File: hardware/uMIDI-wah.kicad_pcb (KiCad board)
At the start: 2 copper layers, 45 x 24 mm, 44 parts, among them Q1 BSS138, U1 TL071CPSR, X1 9V, X2 uMIDI, X3 Input, X4 Output

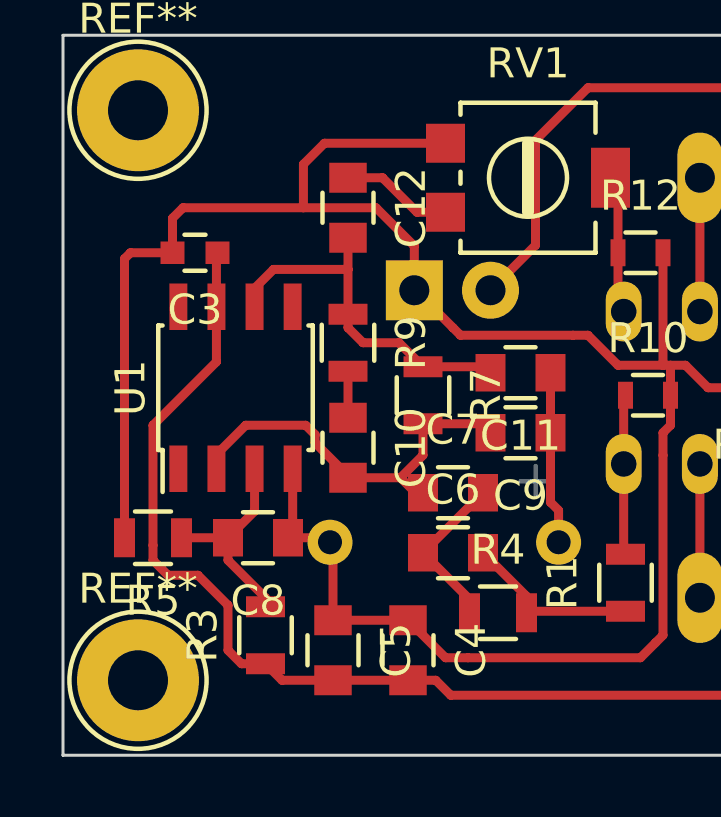
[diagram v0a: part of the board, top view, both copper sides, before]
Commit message: Fix SOIC package width
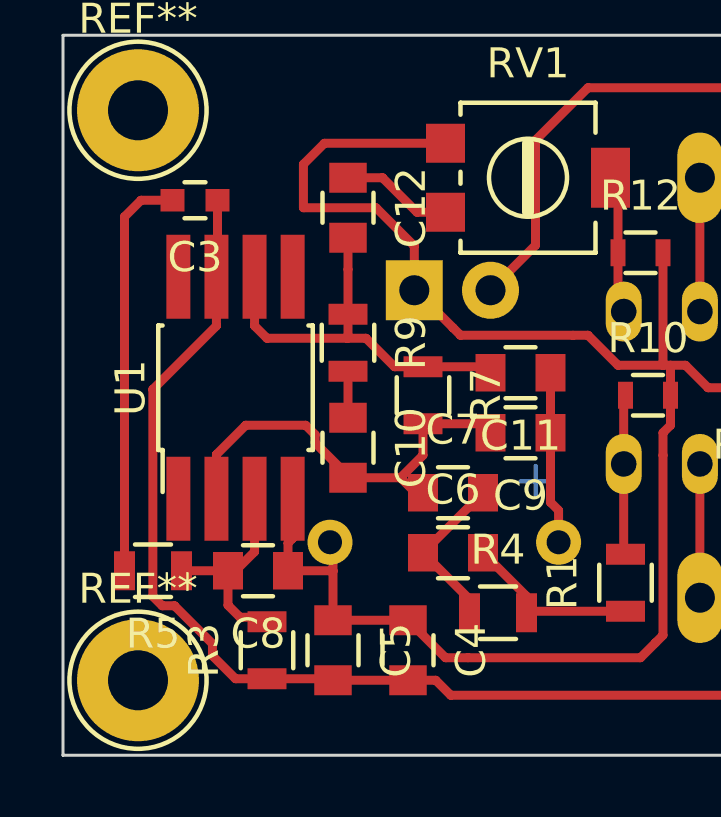
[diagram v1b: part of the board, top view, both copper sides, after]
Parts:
- moved C3 1.75 mm to (184.4, 131.5)
- moved C8 1.10 mm to (186.5, 143.8)
- moved R5 1.10 mm to (183.0, 143.8)
- moved R3 0.50 mm to (186.8, 146.5)
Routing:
- net +9V: track 48.2 -> 51.7 mm
- net Net-(C8-Pad2): track 7.16 -> 9.56 mm
- net GND: track 158.0 -> 155.9 mm
- net Net-(C11-Pad2): track 12.3 -> 13.0 mm

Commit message: Increase pcb size; Add label
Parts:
- added R16: 4.7k, Resistors_SMD:R_0805, F.Cu at (197.0, 123.0)
- C11: value 2n -> 2.2n
- C7: value 47n -> 4.7n
- RV1: value 10k -> 5k
- moved C1 2.00 mm to (208.8, 145.8)
- moved C10 2.00 mm to (191.5, 139.8)
- moved C11 2.00 mm to (197.2, 137.2)
- moved C12 2.00 mm to (191.5, 131.8)
- moved C13 2.00 mm to (214.5, 142.8)
- moved C14 2.00 mm to (210.2, 141.8)
- moved C15 2.00 mm to (218.0, 129.5)
- moved C2 2.00 mm to (210.8, 145.8)
- moved C3 2.00 mm to (186.4, 131.5)
- moved C4 2.00 mm to (193.5, 146.5)
- moved C5 2.00 mm to (191.0, 146.5)
- moved C6 2.00 mm to (195.0, 143.2)
- moved C7 2.00 mm to (195.0, 141.2)
- moved C8 2.00 mm to (188.5, 143.8)
- moved C9 2.00 mm to (197.2, 139.2)
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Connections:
- RV1 pad 1: Net-(C12-Pad1) -> Net-(R16-Pad1)
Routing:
- net Net-(C12-Pad1): track 3.73 -> 0.00 mm
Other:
- board size 45 x 24 mm -> 50 x 24 mm
- board text added: "uMIDI-Wah v0.3"

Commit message: Place and route
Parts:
- removed D1: LED, LEDs:LED-5MM
- removed R2: 82, Resistors_SMD:R_0603
- removed the REF** at (182.5, 147.5)
- removed the REF** at (182.5, 128.5)
- added X5: Enable, Connect:PINHEAD1-2, B.Cu at (223.5, 133.0)
- X2: value uMIDI -> PWM; footprint uMIDI-wah:VASCH5x2_diy-pcb -> Connect:PINHEAD1-2
- moved X2 33.4 mm to (190.0, 129.2), turned to 0 degrees
- moved R6 26.8 mm to (194.2, 129.2), turned to 180 degrees
- moved C15 17.3 mm to (201.5, 134.8), turned to 90 degrees
- moved R15 15.1 mm to (199.5, 134.2), turned to 90 degrees
- moved C1 11.2 mm to (219.5, 142.5), turned to 90 degrees
- moved R16 9.52 mm to (194.8, 132.2)
- moved X1 9.34 mm to (223.5, 143.0), turned to 90 degrees
- moved R14 4.85 mm to (219.0, 132.8), turned to 270 degrees
- moved C2 4.78 mm to (215.5, 146.2), turned to 180 degrees
- moved R4 4.78 mm to (201.2, 144.8), turned to 270 degrees
- moved C6 4.04 mm to (198.8, 144.8), turned to 270 degrees
- moved X4 3.81 mm to (208.0, 129.2)
- moved X3 3.50 mm to (208.0, 144.8)
- moved RV1 3.09 mm to (200.5, 130.0)
- moved R1 3.04 mm to (203.8, 144.8)
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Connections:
- X2 pad 1: (no net) -> GND
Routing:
- net GND: track 155.9 -> 198.5 mm
- net Net-(D2-Pad2): track 21.7 -> 2.35 mm
- net +9V: track 51.7 -> 66.9 mm
- net Net-(C15-Pad2): track 8.10 -> 13.8 mm
- net Net-(C11-Pad2): track 13.0 -> 16.9 mm
- net Net-(C10-Pad2): track 13.2 -> 17.0 mm
- net Net-(C8-Pad2): track 9.56 -> 13.1 mm
- net Net-(C12-Pad1): track 0.00 -> 3.11 mm
- net Net-(D1-Pad2): track 2.85 -> 0.00 mm
- net Net-(R16-Pad1): track 0.00 -> 2.68 mm
- net /True bypass/Loop_Out: track 4.46 -> 6.42 mm
- net /True bypass/relais_p: track 5.78 -> 7.16 mm
- net Net-(C10-Pad1): track 1.55 -> 2.77 mm
- net Net-(C6-Pad2): track 5.92 -> 5.02 mm
- net Net-(C11-Pad1): track 5.76 -> 5.09 mm
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
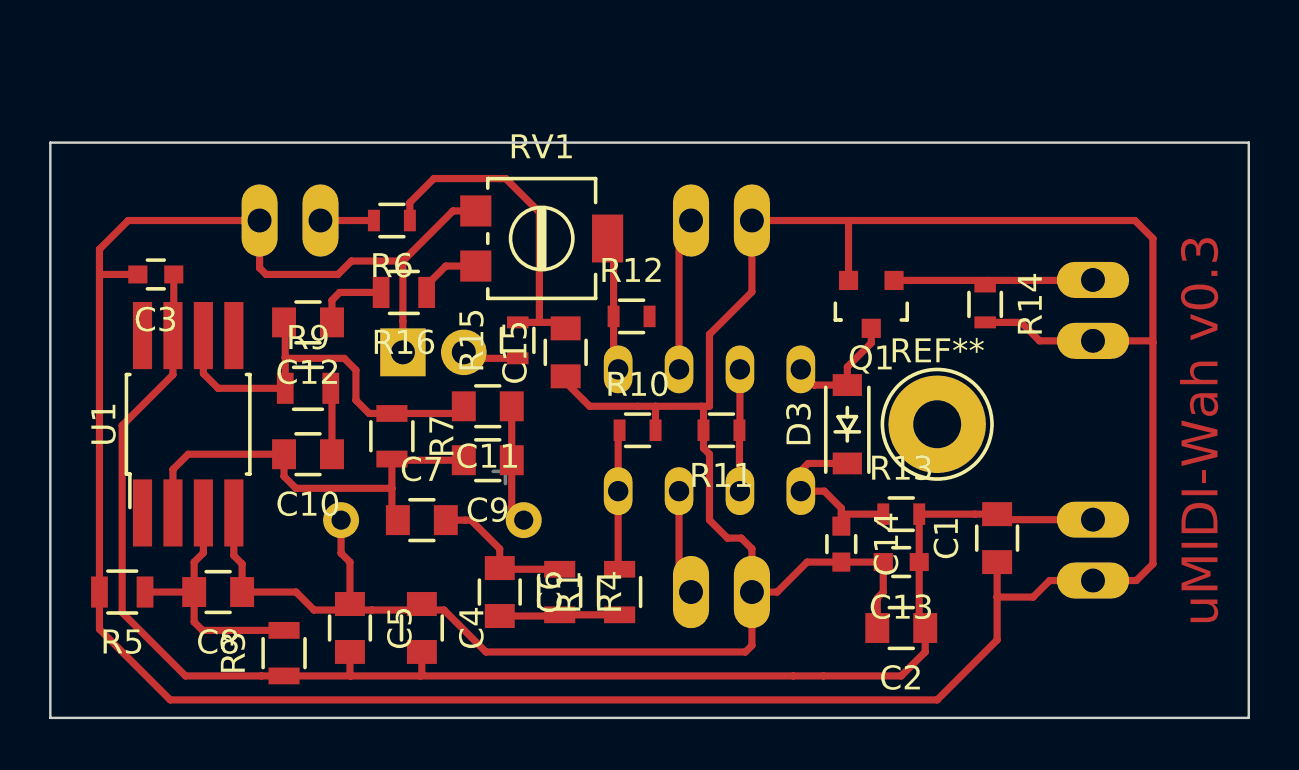
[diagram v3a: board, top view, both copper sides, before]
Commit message: Increase trace widths
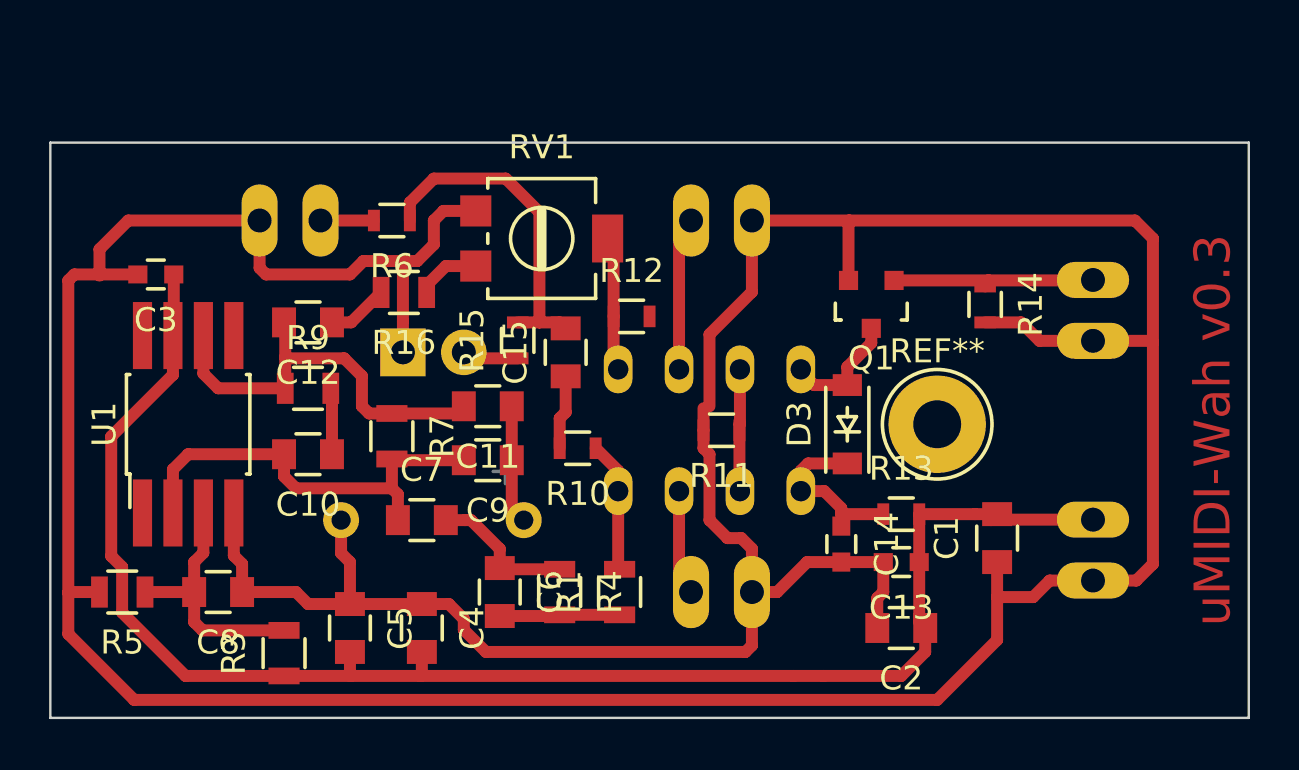
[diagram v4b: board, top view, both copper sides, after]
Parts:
- moved R10 2.61 mm to (202.0, 138.8), turned to 180 degrees
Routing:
- net Net-(C12-Pad1): track 3.11 -> 2.57 mm
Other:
- net class Default: trace_width 0.3 -> 0.5

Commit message: Add 9V polarity protection diode
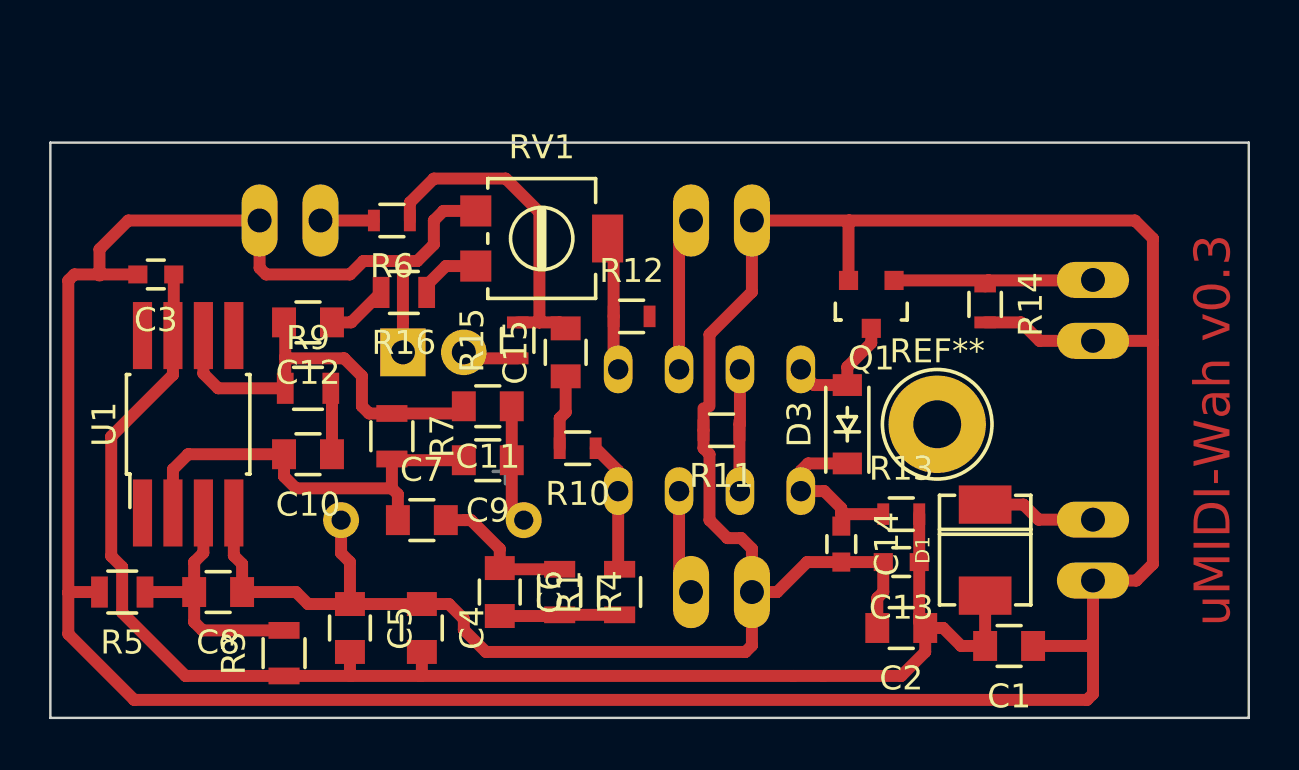
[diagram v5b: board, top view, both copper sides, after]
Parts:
- added D1: B160-13-F, uMIDI:DO-214-AC_SMA, F.Cu at (219.0, 143.0)
- moved C1 4.53 mm to (220.0, 147.0), turned to 180 degrees
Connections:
- X1 pad 2: +9V -> Net-(D1-Pad2)
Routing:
- net Net-(D1-Pad2): track 0.00 -> 4.76 mm
- net GND: track 198.1 -> 200.9 mm
- net +9V: track 67.3 -> 64.5 mm
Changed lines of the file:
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@@
 (kicad_pcb (version 4) (host pcbnew "(2015-09-12 BZR 6188)-product")
   (general
-    (links 72)
+    (links 73)
     (no_connects 0)
     (area 179.949999 125.949999 230.050001 150.050001)
     (thickness 1.6)
     (drawings 7)
-    (tracks 218)
+    (tracks 219)
     (zones 0)
-    (modules 42)
-    (nets 23)
+    (modules 43)
+    (nets 24)
   )
   (page A4)
@@
   (net 21 "Net-(C15-Pad2)")
   (net 22 "Net-(R16-Pad1)")
+  (net 23 "Net-(D1-Pad2)")
   (net_class Default "This is the default net class."
     (clearance 0.3)
@@
     (add_net "Net-(C6-Pad2)")
     (add_net "Net-(C8-Pad2)")
+    (add_net "Net-(D1-Pad2)")
     (add_net "Net-(D2-Pad2)")
     (add_net "Net-(R16-Pad1)")
@@
       (net 1 GND))
     (pad 2 thru_hole oval (at 1.27 0 90) (size 1.50622 3.01498) (drill 0.99822) (layers *.Cu *.Mask)
-      (net 2 +9V))
+      (net 23 "Net-(D1-Pad2)"))
   )
   (module Connect:PINHEAD1-2 (layer B.Cu)
@@
   )
   (module Capacitors_SMD:C_0805 (layer F.Cu)
-    (at 219.5 142.5 90)
+    (at 220 147 180)
     (descr "Capacitor SMD 0805, reflow soldering, AVX (see smccp.pdf)")
     (tags "capacitor 0805")
     (attr smd)
-    (fp_text reference C1 (at 0 -2.1 90) (layer F.SilkS)
-      (effects (font (size 1 1) (thickness 0.15)))
-    )
-    (fp_text value 10u (at 0 2.1 90) (layer F.Fab)
+    (fp_text reference C1 (at 0 -2.1 180) (layer F.SilkS)
+      (effects (font (size 1 1) (thickness 0.15)))
+    )
+    (fp_text value 10u (at 0 2.1 180) (layer F.Fab)
       (effects (font (size 1 1) (thickness 0.15)))
     )
@@
     (fp_line (start 0.5 -0.85) (end -0.5 -0.85) (layer F.SilkS) (width 0.15))
     (fp_line (start -0.5 0.85) (end 0.5 0.85) (layer F.SilkS) (width 0.15))
-    (pad 1 smd rect (at -1 0 90) (size 1 1.25) (layers F.Cu F.Paste F.Mask)
-      (net 1 GND))
-    (pad 2 smd rect (at 1 0 90) (size 1 1.25) (layers F.Cu F.Paste F.Mask)
+    (pad 1 smd rect (at -1 0 180) (size 1 1.25) (layers F.Cu F.Paste F.Mask)
+      (net 1 GND))
+    (pad 2 smd rect (at 1 0 180) (size 1 1.25) (layers F.Cu F.Paste F.Mask)
       (net 2 +9V))
     (model Capacitors_SMD.3dshapes/C_0805.wrl
@@
       (net 16 /PWM))
   )
+  (module uMIDI:DO-214-AC_SMA placed (layer F.Cu)
+    (at 219 143 90)
+    (descr "DO-214AC (SMA)  PACKAGE.")
+    (tags DO-214AC_SMA)
+    (attr smd)
+    (fp_text reference D1 (at 0 -2.60096 90) (layer F.SilkS)
+      (effects (font (size 0.6 0.6) (thickness 0.1143)))
+    )
+    (fp_text value B160-13-F (at 0 2.79908 90) (layer F.SilkS) hide
+      (effects (font (size 1.00076 1.00076) (thickness 0.11938)))
+    )
+    (fp_line (start -2.286 -1.905) (end 2.286 -1.905) (layer F.SilkS) (width 0.15))
+    (fp_line (start 2.286 -1.905) (end 2.286 -1.27) (layer F.SilkS) (width 0.15))
+    (fp_line (start 0.6604 1.905) (end 0.6604 -1.905) (layer F.SilkS) (width 0.15))
+    (fp_line (start 0.8636 1.905) (end 0.8636 -1.905) (layer F.SilkS) (width 0.15))
+    (fp_line (start -2.286 1.27) (end -2.286 1.905) (layer F.SilkS) (width 0.15))
+    (fp_line (start -2.286 1.905) (end 2.286 1.905) (layer F.SilkS) (width 0.15))
+    (fp_line (start 2.286 1.905) (end 2.286 1.27) (layer F.SilkS) (width 0.15))
+    (fp_line (start -2.286 -1.27) (end -2.286 -1.905) (layer F.SilkS) (width 0.15))
+    (pad 1 smd rect (at -1.89992 0 90) (size 1.6002 2.19964) (layers F.Cu F.Paste F.Mask)
+      (net 2 +9V))
+    (pad 2 smd rect (at 1.89992 0 90) (size 1.6002 2.19964) (layers F.Cu F.Paste F.Mask)
+      (net 23 "Net-(D1-Pad2)"))
+    (model smd/do214.wrl
+      (at (xyz 0 0 0))
+      (scale (xyz 0.95 0.95 0.95))
+      (rotate (xyz 0 0 0))
+    )
+  )
   (gr_text "uMIDI-Wah v0.3" (at 228.5 138 90) (layer F.Cu)
     (effects (font (size 1.5 1.5) (thickness 0.35)))
@@
   (gr_line (start 230 126) (end 180 126) (layer Edge.Cuts) (width 0.1))
   (gr_line (start 230 150) (end 180 150) (layer Edge.Cuts) (width 0.1))
+  (segment (start 221 147) (end 223.308637 147) (width 0.5) (layer F.Cu) (net 1))
+  (segment (start 223.308637 147) (end 223.5 146.808637) (width 0.5) (layer F.Cu) (net 1))
+  (segment (start 223.5 149) (end 223.5 146.808637) (width 0.5) (layer F.Cu) (net 1))
+  (segment (start 223.5 146.808637) (end 223.5 144.27) (width 0.5) (layer F.Cu) (net 1))
+  (segment (start 180.75 144.775008) (end 180.75 146.5) (width 0.5) (layer F.Cu) (net 1))
+  (segment (start 180.75 146.5) (end 183.5 149.25) (width 0.5) (layer F.Cu) (net 1))
+  (segment (start 183.5 149.25) (end 223.25 149.25) (width 0.5) (layer F.Cu) (net 1))
+  (segment (start 223.25 149.25) (end 223.5 149) (width 0.5) (layer F.Cu) (net 1))
   (segment (start 201.25 137.5) (end 201.5 137.25) (width 0.5) (layer F.Cu) (net 1))
   (segment (start 201.5 137.25) (end 201.5 135.75) (width 0.5) (layer F.Cu) (net 1))
@@
   (segment (start 198.175 147.25) (end 209 147.25) (width 0.5) (layer F.Cu) (net 1))
   (segment (start 192.5 145.25) (end 195.5 145.25) (width 0.5) (layer F.Cu) (net 1))
-  (segment (start 180.75 144.775008) (end 180.75 146.5) (width 0.5) (layer F.Cu) (net 1))
-  (segment (start 180.75 146.5) (end 183.5 149.25) (width 0.5) (layer F.Cu) (net 1))
-  (segment (start 183.5 149.25) (end 217 149.25) (width 0.5) (layer F.Cu) (net 1))
-  (segment (start 217 149.25) (end 219.5 146.75) (width 0.5) (layer F.Cu) (net 1))
-  (segment (start 219.5 146.75) (end 219.5 144.960213) (width 0.5) (layer F.Cu) (net 1))
   (segment (start 180.75 131.75) (end 180.75 144.775008) (width 0.5) (layer F.Cu) (net 1))
   (segment (start 182.05 144.75) (end 180.775008 144.75) (width 0.5) (layer F.Cu) (net 1))
@@
   (segment (start 194.71 130.94) (end 194.71 133.45) (width 0.5) (layer F.Cu) (net 1))
   (segment (start 194.71 133.45) (end 194.71 134.75) (width 0.5) (layer F.Cu) (net 1))
-  (segment (start 219.5 143.5) (end 219.5 144.960213) (width 0.5) (layer F.Cu) (net 1))
-  (segment (start 223.5 144.27) (end 221.69251 144.27) (width 0.5) (layer F.Cu) (net 1))
-  (segment (start 221.69251 144.27) (end 221.002297 144.960213) (width 0.5) (layer F.Cu) (net 1))
-  (segment (start 221.002297 144.960213) (end 219.5 144.960213) (width 0.5) (layer F.Cu) (net 1))
   (segment (start 182.05 131.546616) (end 182.05 130.45) (width 0.5) (layer F.Cu) (net 1))
   (segment (start 183.65 131.5) (end 182.096616 131.5) (width 0.5) (layer F.Cu) (net 1))
@@
   (segment (start 188 143.575) (end 187.655 143.23) (width 0.5) (layer F.Cu) (net 1))
   (segment (start 187.655 143.23) (end 187.655 140.45) (width 0.5) (layer F.Cu) (net 1))
+  (segment (start 219 147) (end 218 147) (width 0.5) (layer F.Cu) (net 2))
+  (segment (start 218 147) (end 217.25 146.25) (width 0.5) (layer F.Cu) (net 2))
+  (segment (start 217.25 146.25) (end 216.5 146.25) (width 0.5) (layer F.Cu) (net 2))
+  (segment (start 219 144.64992) (end 219 146.75) (width 0.5) (layer F.Cu) (net 2))
   (segment (start 189.75 148.25) (end 185.639998 148.25) (width 0.5) (layer F.Cu) (net 2))
   (segment (start 185.639998 148.25) (end 182.994999 145.605001) (width 0.5) (layer F.Cu) (net 2))
@@
   (segment (start 216.25 146) (end 216.5 146.25) (width 0.5) (layer F.Cu) (net 2))
   (segment (start 216.25 143.5) (end 216.25 141.5) (width 0.5) (layer F.Cu) (net 2))
-  (segment (start 219.5 141.5) (end 218.575 141.5) (width 0.5) (layer F.Cu) (net 2))
-  (segment (start 218.575 141.5) (end 216.25 141.5) (width 0.5) (layer F.Cu) (net 2))
-  (segment (start 219.25 141.75) (end 219.5 141.5) (width 0.5) (layer F.Cu) (net 2))
-  (segment (start 223.5 141.73) (end 219.73 141.73) (width 0.5) (layer F.Cu) (net 2))
-  (segment (start 219.73 141.73) (end 219.5 141.5) (width 0.5) (layer F.Cu) (net 2))
   (segment (start 185.115 135.05) (end 185.15 135.015) (width 0.5) (layer F.Cu) (net 2))
   (segment (start 185.15 135.015) (end 185.15 131.5) (width 0.5) (layer F.Cu) (net 2))
@@
   (segment (start 195.7 131.95) (end 196.5 131.15) (width 0.5) (layer F.Cu) (net 22))
   (segment (start 196.5 131.15) (end 197.75 131.15) (width 0.5) (layer F.Cu) (net 22))
+  (segment (start 220.60008 141.10008) (end 221.23 141.73) (width 0.5) (layer F.Cu) (net 23))
+  (segment (start 221.23 141.73) (end 223.5 141.73) (width 0.5) (layer F.Cu) (net 23))
+  (segment (start 219 141.10008) (end 220.60008 141.10008) (width 0.5) (layer F.Cu) (net 23))
   (zone (net 1) (net_name GND) (layer F.Cu) (hatch edge 0.508)
     (connect_pads (clearance 0.4))
